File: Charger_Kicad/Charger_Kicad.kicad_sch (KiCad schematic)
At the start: 12 parts

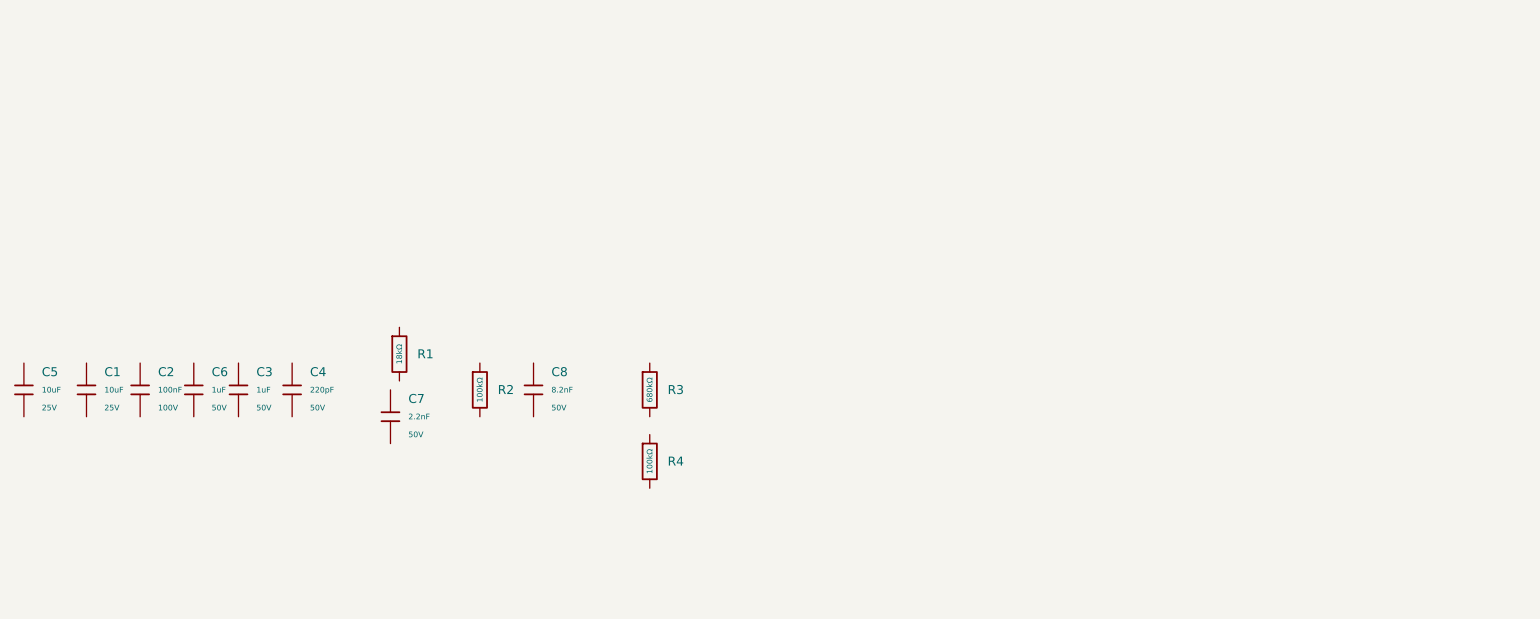
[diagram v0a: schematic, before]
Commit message: Updated to use ISP5328P breakout, created initial case CAD
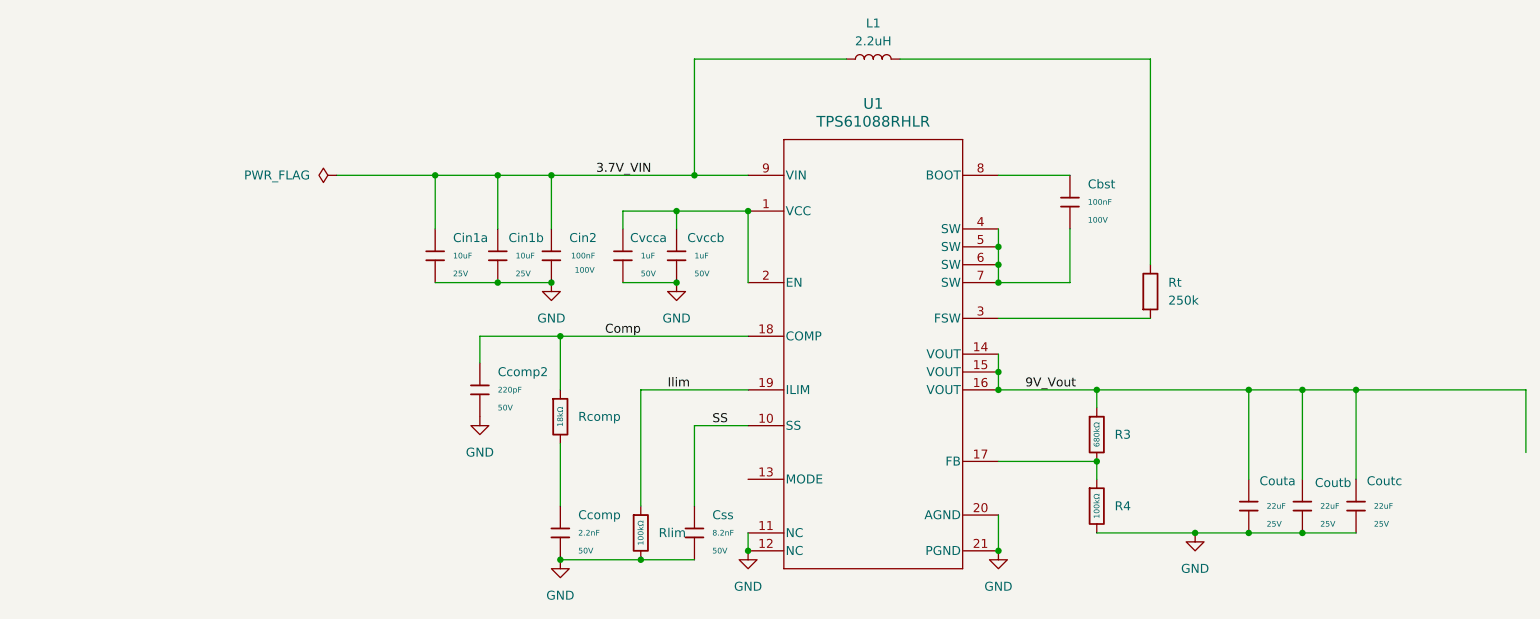
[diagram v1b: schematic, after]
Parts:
- removed C3: 1uF, PCM_JLCPCB:C_0805, symbol PCM_JLCPCB-Capacitors:0805,1uF
- added Cbst: 100nF, PCM_JLCPCB:C_0805, symbol PCM_JLCPCB-Capacitors:0805,100nF
- added Couta, Coutb, Coutc: 22uF, PCM_JLCPCB:C_0805, symbol PCM_JLCPCB-Capacitors:0805,22uF
- added Cvccb: 1uF, PCM_JLCPCB:C_0805, symbol PCM_JLCPCB-Capacitors:0805,1uF
- added L1: 2.2uH, symbol Device:L
- added Rt: 250k, symbol Device:R
- added U1: TPS61088RHLR, RHL0020A, symbol 2026-02-10_20-55-32:TPS61088RHLR
- renumbered C7 to Ccomp, C4 to Ccomp2, C5 to Cin1a, C1 to Cin1b, C2 to Cin2, C8 to Css, C6 to Cvcca, R1 to Rcomp, R2 to Rlim
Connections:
- net 3.7V_VIN: now reaches Cin1a.1
- net 3.7V_VIN: now also Cin1b.1, Cin2.1, L1.1, U1.9 (VIN)
- net GND: now reaches Cin1a.2
- net GND: now also Ccomp.2, Ccomp2.2, Cin1b.2, Cin2.2, Css.2, Cvcca.2, R4.2, Rlim.2, Couta.2, Coutb.2, Coutc.2, Cvccb.2, U1.11 (NC), U1.12 (NC), U1.20 (AGND), U1.21 (PGND)
- net at Ccomp.1: now also Rcomp.2
- net Comp: now reaches Ccomp2.1
- net Comp: now also Rcomp.1, U1.18 (COMP)
- net 9V_Vout: now reaches R3.1
- net 9V_Vout: now also Couta.1, Coutb.1, Coutc.1, U1.14 (VOUT), U1.15 (VOUT), U1.16 (VOUT)
- net at R3.2: now also R4.1, U1.17 (FB)
- net Ilim: now reaches Rlim.1
- net Ilim: now also U1.19 (ILIM)
- net SS: now reaches Css.1
- net SS: now also U1.10 (SS)
- net at Cvcca.1: now also Cvccb.1, U1.1 (VCC), U1.2 (EN)
- new net: L1.2, Rt.1
- new net: Cbst.1, U1.8 (BOOT)
- new net: Cbst.2, U1.4 (SW), U1.5 (SW), U1.6 (SW), U1.7 (SW)
- new net: Rt.2, U1.3 (FSW)
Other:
- moved on the sheet: Ccomp, Ccomp2, Cin1a, Cin1b, Cin2, Css, Cvcca, R3, R4, Rcomp, Rlim
